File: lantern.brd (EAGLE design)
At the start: 50 x 40 mm, 39 parts, among them T1 2N2222B, T2 2N2222B, T3 2N2222B, T4_2SC2120Y 2N2222B, T5_2SA950 2N2907, U2 HT7733A

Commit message: RevA pcb finished, first case version
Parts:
- removed T4_2SC2120Y: 2N2222B, blinkinlabs:SOT23
- removed T5_2SA950: 2N2907, adafruit:TO92-EBC-OVAL
- added GAIN: AYZ0202, SparkFun-Electromechanical:AYZ0202
- added R15, R16: 15K, adafruit:R0603
- added T4: 2N2222B, blinkinlabs:SOT23
- added T5: 2N2907B, blinkinlabs:SOT23
- moved U$1 6.32 mm to (15.0, 6.00), turned to 180 degrees
- moved C1 6.00 mm to (21.0, 6.00)
- moved ON/OFF 6.00 mm to (6.00, 13.0)
- moved R3 6.00 mm to (24.0, 9.00)
- moved R4 6.00 mm to (24.0, 6.00)
- moved C7 5.10 mm to (33.0, 13.0)
- moved BAT1 5.00 mm to (25.0, 29.0)
- moved C2 5.00 mm to (25.0, 3.00)
- moved C3 5.00 mm to (32.0, 3.00)
- moved C4 5.00 mm to (35.0, 7.00)
- moved C5 5.00 mm to (42.0, 4.00)
- moved C6 5.00 mm to (45.0, 23.0)
- moved D1 5.00 mm to (11.0, 22.0)
- moved D2 5.00 mm to (41.0, 23.0)
- moved D3 5.00 mm to (39.0, 4.00)
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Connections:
- new net N$22: GAIN.4, R16.2
- new net N$23: GAIN.1, R15.2
- net DGND: now also T4.2; no longer T4_2SC2120Y.2
- net GND: now also T4.3; no longer T4_2SC2120Y.3
- net N$13: now also T5.3; no longer T5_2SA950.C
- net N$14: now also T4.1; no longer T4_2SC2120Y.1
- net N$15: now also T5.2; no longer T5_2SA950.E
- net N$16: now also T5.1; no longer T5_2SA950.B
- net N$4: now also R16.1
- net N$5: now also R15.1
- net VCC: now also GAIN.2, GAIN.5
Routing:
- net N$22: track 0.00 -> 42.3 mm, vias 0 -> 2
- net VCC: track 60.0 -> 84.5 mm
- net N$23: track 0.00 -> 23.6 mm, vias 0 -> 2
- net GND: track 25.5 -> 8.51 mm, vias 0 -> 8
- net N$15: track 35.0 -> 41.8 mm
- net N$7: track 12.9 -> 6.08 mm
- net N$13: track 32.5 -> 38.3 mm, vias 1 -> 2
- net N$8: track 32.5 -> 27.4 mm
- net N$21: track 15.3 -> 11.1 mm
- net N$16: track 7.25 -> 3.87 mm, vias 1 -> 0
- net N$5: track 6.11 -> 8.26 mm
- net N$4: track 10.3 -> 11.7 mm
- net N$17: track 44.9 -> 45.5 mm
- net N$20: track 6.24 -> 5.74 mm
- net N$19: track 5.42 -> 4.92 mm
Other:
- board size 50 x 40 mm -> 50 x 35 mm
- board text added: "Be blinkin awesome"
- board text added: "Disco"
- board text added: "Honghong"
- board text added: "Lantern"
- board text added: "Matt"
- board text added: "Solar"
- board text added: "and"
- board text removed: "Honghong and Matt"

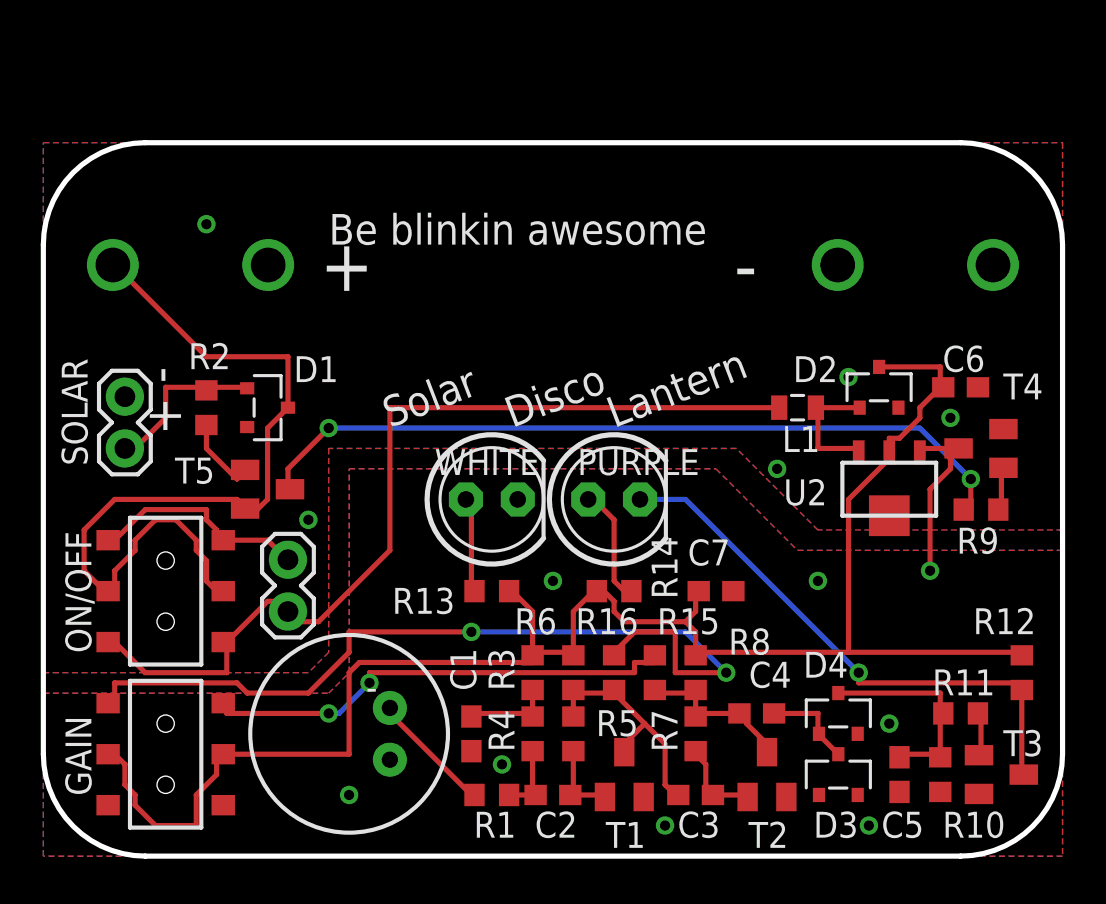
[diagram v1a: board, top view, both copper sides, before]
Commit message: Small updates for RevB, change capacitor size and fix some labels. Hope it works!
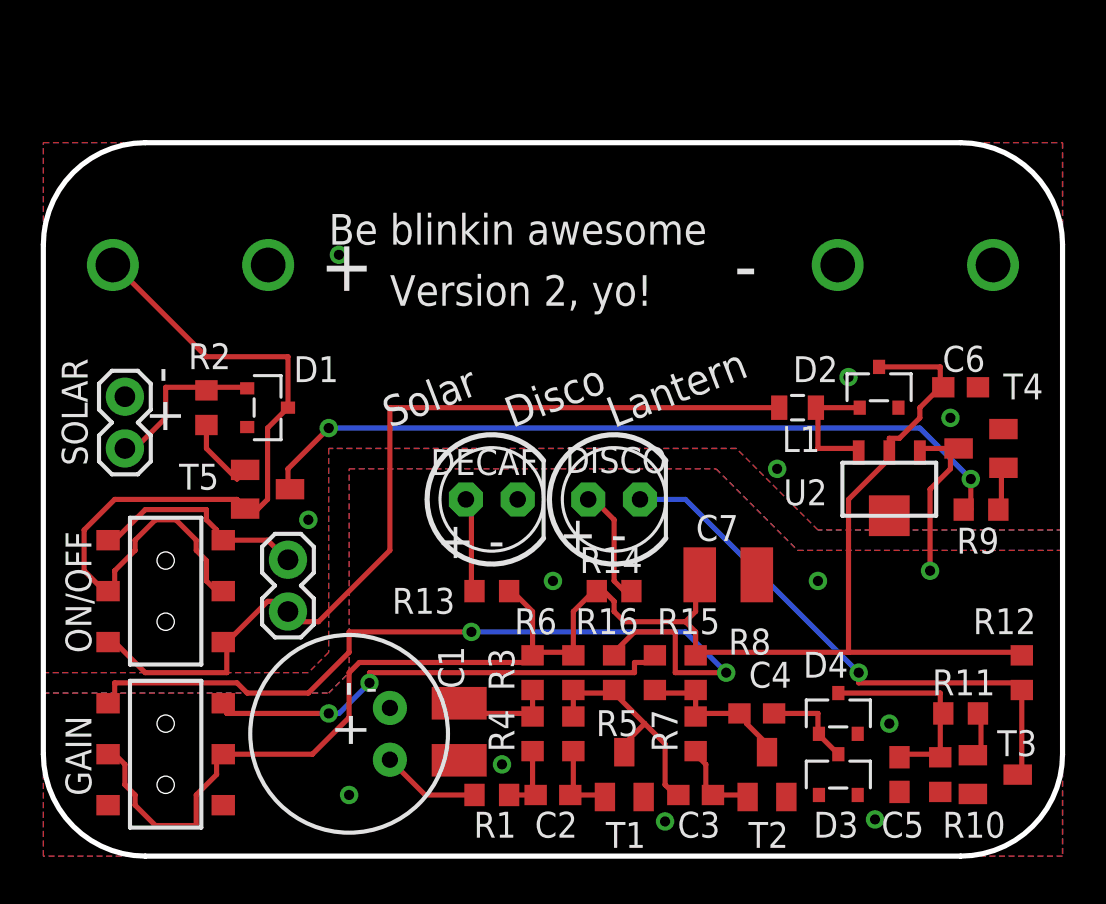
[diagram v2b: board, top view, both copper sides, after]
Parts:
- C1, C7: device adafruit:C0603 -> adafruit:C1210
- LED1: value PURPLE -> DISCO
- LED2: value WHITE -> DECAF
- R11: value 1M -> 39k
- R14: value 100 -> 0
- R2, R9: value 1k -> 1.2k
- R6, R8: value 39K -> 51K
- moved C7 1.00 mm to (33.6, 13.8)
- moved C1 0.61 mm to (20.4, 6.10)
- moved T3 0.30 mm to (46.7, 4.00)
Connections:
- net GND: now also U$1.2; no longer U$1.1
- net N$7: now also U$1.1; no longer U$1.2
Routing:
- net N$7: track 6.08 -> 4.87 mm
- net N$2: track 4.45 -> 5.08 mm
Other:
- board text added: "!!SOLAR DISCO LANTERN!!"
- board text added: "- +"
- board text added: "DISCO DISCO DISCO DISCO"
- board text added: "Version 2, yo!"
- board text added: "With Love From"
